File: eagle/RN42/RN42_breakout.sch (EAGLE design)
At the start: 15 parts

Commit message: Update RN42 breakout board.
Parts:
- removed U$3, U$4: N-CHANNEL-MOSFET-BSS138, GeekAmmo:N-CHANNEL-MOSFET-BSS138
- added L2, L3: (no value), led:LEDCHIPLED_0603
- added R6, R7: 1k, rcl:R-EU_R0603
- added SJ1, SJ2, SJ3, SJ4: (no value), jumper:SJ
- added T1: N-MOSFET, GeekAmmo:N-CHANNEL-MOSFET-BSS138
- added T2: N-CHANNEL-MOSFET-BSS138, GeekAmmo:N-CHANNEL-MOSFET-BSS138
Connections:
- removed net LINK: U$1.UARTCTS, U$1.UARTRTS
- new net AUTODISCOVERY: SJ3.1, U$1.PIO3
- new net BD_RATE: SJ4.1, U$1.PIO7
- new net BT_MASTER: SJ1.1, U$1.PIO6
- new net CTS: J1.3, U$1.UARTCTS
- new net N$3: L2.A, R6.2
- new net N$4: L3.A, R7.1
- new net RTS: J1.4, U$1.UARTRTS
- net 3V3: now also R7.2, SJ1.2, SJ3.2, SJ4.2, T1.G, T2.G; no longer U$3.G, U$4.G
- net GND: now also J1.1, L2.C, L3.C, SJ2.2; no longer J1.3, U$1.PIO7
- net RESET: now also SJ2.1; no longer J1.1
- net RX: now also T2.S; no longer U$3.S
- net RXH: now also T2.D; no longer U$3.D
- net STATUS: now also R6.1; no longer J1.4
- net TX: now also T1.S; no longer U$4.S
- net TXH: now also T1.D; no longer U$4.D
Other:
- note added: "Power Status"
- note added: "Reset (low power operation)"
- note added: "VCC to 3V3"
- moved on the sheet: L1, R1, R2, R3, R4, R5, U$1

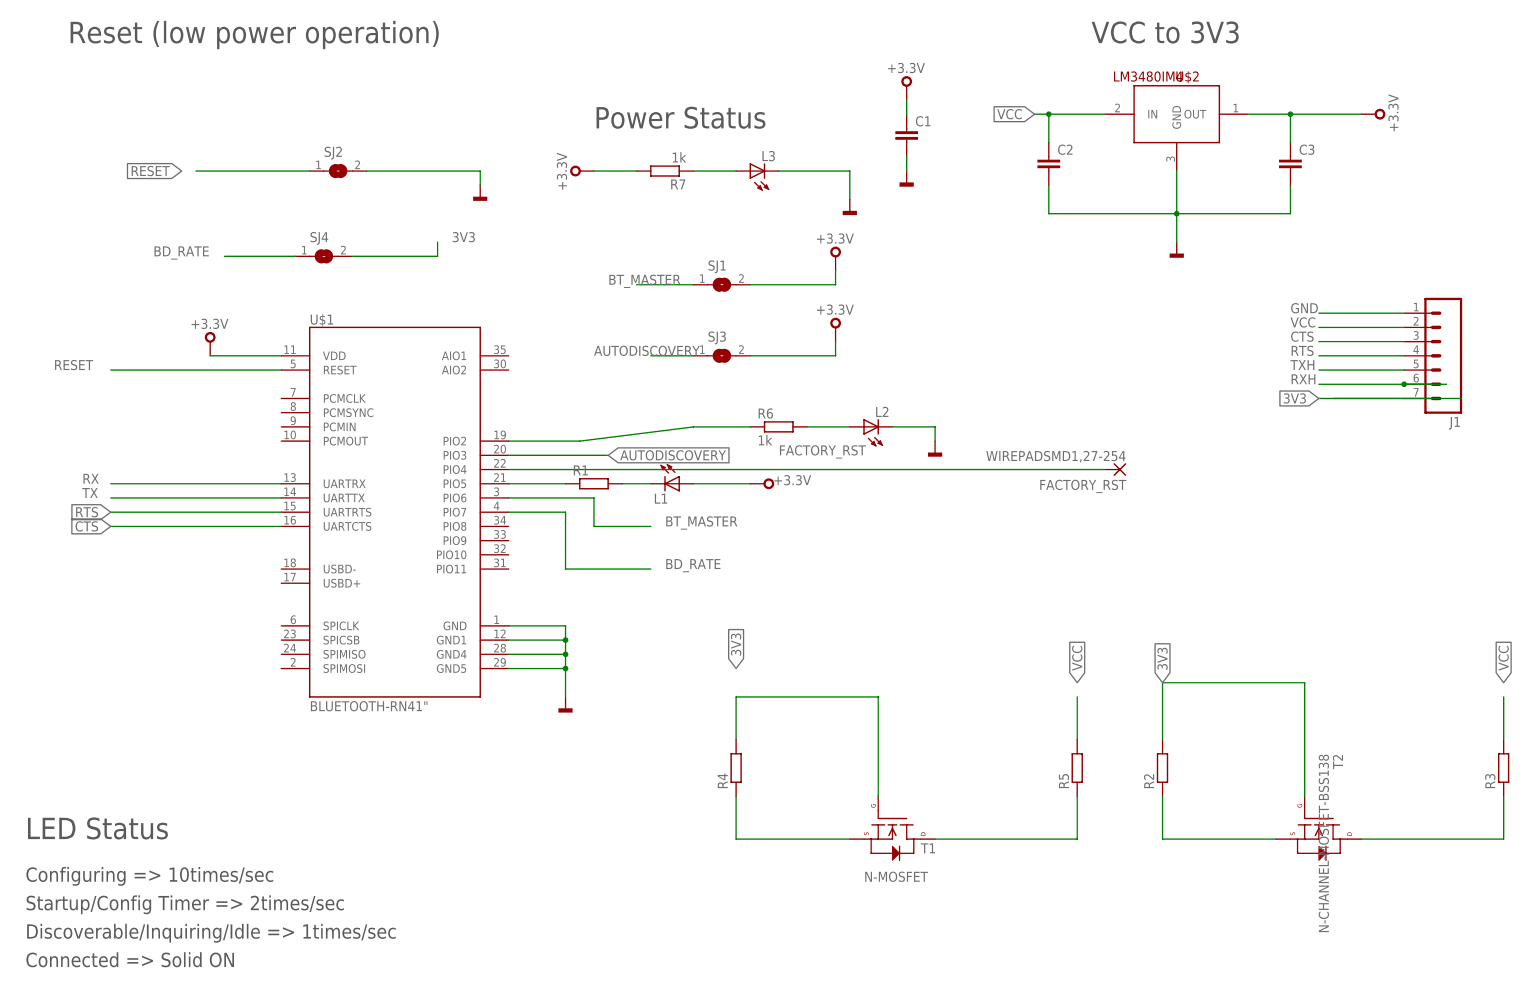
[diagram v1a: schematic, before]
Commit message: Pratically completed layout for RN42 breakout.
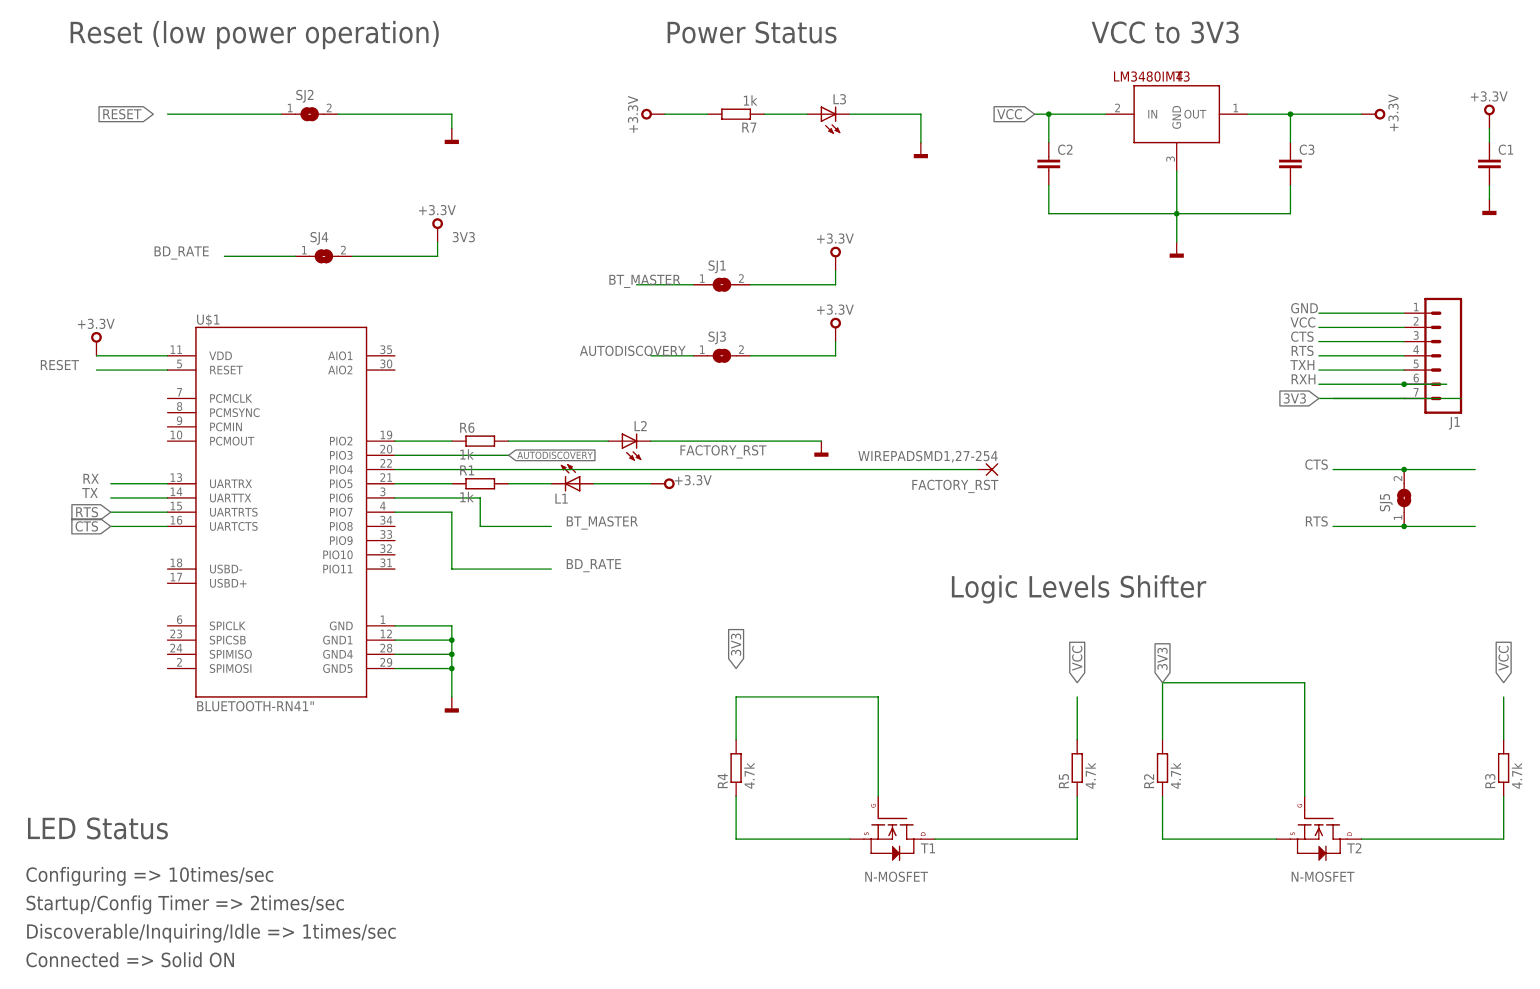
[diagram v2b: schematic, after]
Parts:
- added SJ5: (no value), jumper:SJ
- R1: value (none) -> 1k
- R2, R3, R4, R5: value (none) -> 4.7k
- T2: value N-CHANNEL-MOSFET-BSS138 -> N-MOSFET
- renumbered U$2 to T3
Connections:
- net CTS: now also SJ5.2
- net RTS: now also SJ5.1
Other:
- note added: "Logic Levels Shifter"
- moved on the sheet: C1, FACTORY_RST, L1, L2, L3, R1, R6, R7, SJ2, U$1

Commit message: Fix some labels on RN42 breakout.
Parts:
- renumbered L1 to STATUS, L2 to CONN, SJ1 to MASTER, SJ2 to POWER, SJ3 to AUTODISCOVERY, SJ4 to BAUD
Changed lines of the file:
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@@
 <part name="FACTORY_RST" library="wirepad" deviceset="WIREPAD" device="SMD1,27-254" value="WIREPADSMD1,27-254"/>
 <part name="U$1" library="SparkFun" deviceset="BLUETOOTH-RN41" device="&quot;"/>
-<part name="L1" library="led" deviceset="LED" device="CHIPLED_0603"/>
+<part name="STATUS" library="led" deviceset="LED" device="CHIPLED_0603"/>
 <part name="T3" library="SparkFun-PowerIC" deviceset="LM3480IM4" device=""/>
 <part name="C2" library="SparkFun-Passives" deviceset="CAP" device="0603-CAP"/>
@@
 </part>
 <part name="R6" library="rcl" deviceset="R-EU_" device="R0603" value="1k"/>
-<part name="L2" library="led" deviceset="LED" device="CHIPLED_0603"/>
+<part name="CONN" library="led" deviceset="LED" device="CHIPLED_0603"/>
 <part name="GND5" library="mbed-power" deviceset="GND" device=""/>
 <part name="U+3" library="mbed-power" deviceset="+3.3V" device=""/>
@@
 <part name="L3" library="led" deviceset="LED" device="CHIPLED_0603"/>
 <part name="GND7" library="mbed-power" deviceset="GND" device=""/>
-<part name="SJ1" library="jumper" deviceset="SJ" device=""/>
+<part name="MASTER" library="jumper" deviceset="SJ" device=""/>
 <part name="3V3" library="mbed-power" deviceset="+3.3V" device=""/>
-<part name="SJ2" library="jumper" deviceset="SJ" device=""/>
-<part name="SJ3" library="jumper" deviceset="SJ" device=""/>
+<part name="POWER" library="jumper" deviceset="SJ" device=""/>
+<part name="AUTODISCOVERY" library="jumper" deviceset="SJ" device=""/>
 <part name="3V1" library="mbed-power" deviceset="+3.3V" device=""/>
-<part name="SJ4" library="jumper" deviceset="SJ" device=""/>
+<part name="BAUD" library="jumper" deviceset="SJ" device=""/>
 <part name="SJ5" library="jumper" deviceset="SJ" device=""/>
 <part name="3V2" library="mbed-power" deviceset="+3.3V" device=""/>
@@
 </instance>
 <instance part="U$1" gate="G$1" x="55.88" y="101.6"/>
-<instance part="L1" gate="G$1" x="109.22" y="106.68" rot="R270"/>
+<instance part="STATUS" gate="G$1" x="109.22" y="106.68" rot="R270"/>
 <instance part="T3" gate="G$1" x="215.9" y="172.72"/>
 <instance part="C2" gate="G$1" x="193.04" y="162.56"/>
@@
 </instance>
 <instance part="R6" gate="G$1" x="91.44" y="114.3"/>
-<instance part="L2" gate="G$1" x="116.84" y="114.3" rot="R90"/>
+<instance part="CONN" gate="G$1" x="116.84" y="114.3" rot="R90"/>
 <instance part="GND5" gate="1" x="152.4" y="114.3"/>
 <instance part="U+3" gate="1" x="124.46" y="172.72" rot="R90"/>
@@
 <instance part="L3" gate="G$1" x="152.4" y="172.72" rot="R90"/>
 <instance part="GND7" gate="1" x="86.36" y="170.18"/>
-<instance part="SJ1" gate="1" x="134.62" y="142.24"/>
+<instance part="MASTER" gate="1" x="134.62" y="142.24"/>
 <instance part="3V3" gate="1" x="154.94" y="144.78"/>
-<instance part="SJ2" gate="1" x="60.96" y="172.72"/>
-<instance part="SJ3" gate="1" x="134.62" y="129.54"/>
+<instance part="POWER" gate="1" x="60.96" y="172.72"/>
+<instance part="AUTODISCOVERY" gate="1" x="134.62" y="129.54"/>
 <instance part="3V1" gate="1" x="154.94" y="132.08"/>
-<instance part="SJ4" gate="1" x="63.5" y="147.32"/>
+<instance part="BAUD" gate="1" x="63.5" y="147.32"/>
 <instance part="SJ5" gate="1" x="256.54" y="104.14" rot="R90"/>
 <instance part="3V2" gate="1" x="83.82" y="149.86"/>
@@
 <segment>
 <pinref part="GND5" gate="1" pin="GND"/>
-<pinref part="L2" gate="G$1" pin="C"/>
+<pinref part="CONN" gate="G$1" pin="C"/>
 <wire x1="121.92" y1="114.3" x2="152.4" y2="114.3" width="0.1524" layer="91"/>
 </segment>
@@
 <wire x1="86.36" y1="172.72" x2="86.36" y2="170.18" width="0.1524" layer="91"/>
 <pinref part="GND7" gate="1" pin="GND"/>
-<pinref part="SJ2" gate="1" pin="2"/>
+<pinref part="POWER" gate="1" pin="2"/>
 <wire x1="86.36" y1="172.72" x2="66.04" y2="172.72" width="0.1524" layer="91"/>
 </segment>
@@
 <wire x1="55.88" y1="172.72" x2="35.56" y2="172.72" width="0.1524" layer="91"/>
 <label x="33.02" y="172.72" size="1.778" layer="95" rot="R180" xref="yes"/>
-<pinref part="SJ2" gate="1" pin="1"/>
+<pinref part="POWER" gate="1" pin="1"/>
 </segment>
 </net>
@@
 <wire x1="104.14" y1="106.68" x2="96.52" y2="106.68" width="0.1524" layer="91"/>
 <pinref part="R1" gate="G$1" pin="2"/>
-<pinref part="L1" gate="G$1" pin="C"/>
+<pinref part="STATUS" gate="G$1" pin="C"/>
 </segment>
 </net>
@@
 <wire x1="121.92" y1="106.68" x2="111.76" y2="106.68" width="0.1524" layer="91"/>
 <pinref part="U+2" gate="1" pin="+3,3V"/>
-<pinref part="L1" gate="G$1" pin="A"/>
+<pinref part="STATUS" gate="G$1" pin="A"/>
 </segment>
 <segment>
@@
 </segment>
 <segment>
-<pinref part="SJ1" gate="1" pin="2"/>
+<pinref part="MASTER" gate="1" pin="2"/>
 <wire x1="139.7" y1="142.24" x2="154.94" y2="142.24" width="0.1524" layer="91"/>
 <wire x1="154.94" y1="142.24" x2="154.94" y2="144.78" width="0.1524" layer="91"/>
@@
 </segment>
 <segment>
-<pinref part="SJ3" gate="1" pin="2"/>
+<pinref part="AUTODISCOVERY" gate="1" pin="2"/>
 <wire x1="139.7" y1="129.54" x2="154.94" y2="129.54" width="0.1524" layer="91"/>
 <wire x1="154.94" y1="129.54" x2="154.94" y2="132.08" width="0.1524" layer="91"/>
@@
 </segment>
 <segment>
-<pinref part="SJ4" gate="1" pin="2"/>
+<pinref part="BAUD" gate="1" pin="2"/>
 <wire x1="68.58" y1="147.32" x2="83.82" y2="147.32" width="0.1524" layer="91"/>
 <wire x1="83.82" y1="147.32" x2="83.82" y2="149.86" width="0.1524" layer="91"/>
@@
 <segment>
 <pinref part="R6" gate="G$1" pin="2"/>
-<pinref part="L2" gate="G$1" pin="A"/>
+<pinref part="CONN" gate="G$1" pin="A"/>
 <wire x1="96.52" y1="114.3" x2="114.3" y2="114.3" width="0.1524" layer="91"/>
 </segment>
@@
 </segment>
 <segment>
-<pinref part="SJ3" gate="1" pin="1"/>
+<pinref part="AUTODISCOVERY" gate="1" pin="1"/>
 <wire x1="129.54" y1="129.54" x2="121.92" y2="129.54" width="0.1524" layer="91"/>
 <label x="109.22" y="129.54" size="1.778" layer="95"/>
@@
 </segment>
 <segment>
-<pinref part="SJ1" gate="1" pin="1"/>
+<pinref part="MASTER" gate="1" pin="1"/>
 <wire x1="129.54" y1="142.24" x2="119.38" y2="142.24" width="0.1524" layer="91"/>
 <label x="114.3" y="142.24" size="1.778" layer="95"/>
@@
 </segment>
 <segment>
-<pinref part="SJ4" gate="1" pin="1"/>
+<pinref part="BAUD" gate="1" pin="1"/>
 <wire x1="58.42" y1="147.32" x2="45.72" y2="147.32" width="0.1524" layer="91"/>
 <label x="33.02" y="147.32" size="1.778" layer="95"/>

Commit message: Complete first release
Add production file.
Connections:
- net CTS: no longer J1.3
- net GND: now also J1.3; no longer J1.1
- net RTS: no longer J1.4
- net VCC: now also J1.4; no longer J1.2
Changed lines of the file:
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@@
 </segment>
 <segment>
-<pinref part="J1" gate="G$1" pin="1"/>
-<wire x1="256.54" y1="137.16" x2="241.3" y2="137.16" width="0.1524" layer="91"/>
+<pinref part="J1" gate="G$1" pin="3"/>
+<wire x1="256.54" y1="132.08" x2="241.3" y2="137.16" width="0.1524" layer="91"/>
 <label x="236.22" y="137.16" size="1.778" layer="95"/>
 </segment>
@@
 </segment>
 <segment>
-<pinref part="J1" gate="G$1" pin="4"/>
-<wire x1="256.54" y1="129.54" x2="241.3" y2="129.54" width="0.1524" layer="91"/>
-<label x="236.22" y="129.54" size="1.778" layer="95"/>
-</segment>
-<segment>
 <pinref part="SJ5" gate="1" pin="1"/>
 <wire x1="243.84" y1="99.06" x2="256.54" y2="99.06" width="0.1524" layer="91"/>
-<wire x1="256.54" y1="99.06" x2="269.24" y2="99.06" width="0.1524" layer="91"/>
-<junction x="256.54" y="99.06"/>
 <label x="238.76" y="99.06" size="1.778" layer="95"/>
 </segment>
@@
 </segment>
 <segment>
-<pinref part="J1" gate="G$1" pin="2"/>
-<wire x1="256.54" y1="134.62" x2="241.3" y2="134.62" width="0.1524" layer="91"/>
+<pinref part="J1" gate="G$1" pin="4"/>
+<wire x1="256.54" y1="129.54" x2="241.3" y2="134.62" width="0.1524" layer="91"/>
 <label x="236.22" y="134.62" size="1.778" layer="95"/>
 </segment>
@@
 <pinref part="J1" gate="G$1" pin="7"/>
 <wire x1="256.54" y1="121.92" x2="243.84" y2="121.92" width="0.1524" layer="91"/>
-<wire x1="256.54" y1="121.92" x2="266.7" y2="121.92" width="0.1524" layer="91"/>
 <wire x1="256.54" y1="121.92" x2="241.3" y2="121.92" width="0.1524" layer="91"/>
 <label x="241.3" y="121.92" size="1.778" layer="95" rot="R180" xref="yes"/>
@@
 <net name="RXH" class="0">
 <segment>
-<wire x1="264.16" y1="124.46" x2="256.54" y2="124.46" width="0.1524" layer="91"/>
 <label x="236.22" y="124.46" size="1.778" layer="95"/>
 <pinref part="J1" gate="G$1" pin="6"/>
-<junction x="256.54" y="124.46"/>
 <wire x1="256.54" y1="124.46" x2="241.3" y2="124.46" width="0.1524" layer="91"/>
 </segment>
@@
 </segment>
 <segment>
-<pinref part="J1" gate="G$1" pin="3"/>
-<wire x1="256.54" y1="132.08" x2="241.3" y2="132.08" width="0.1524" layer="91"/>
-<label x="236.22" y="132.08" size="1.778" layer="95"/>
-</segment>
-<segment>
 <pinref part="SJ5" gate="1" pin="2"/>
 <wire x1="243.84" y1="109.22" x2="256.54" y2="109.22" width="0.1524" layer="91"/>
-<wire x1="256.54" y1="109.22" x2="269.24" y2="109.22" width="0.1524" layer="91"/>
-<junction x="256.54" y="109.22"/>
 <label x="238.76" y="109.22" size="1.778" layer="95"/>
 </segment>

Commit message: RN42: update some values.
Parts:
- C1: value (none) -> 1uF
- C2, C3: value (none) -> 0.1uF
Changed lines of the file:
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@@
 <?xml version="1.0" encoding="utf-8"?>
 <!DOCTYPE eagle SYSTEM "eagle.dtd">
-<eagle version="7.2.0">
+<eagle version="7.5.0">
 <drawing>
 <settings>
@@
 <part name="R1" library="rcl" deviceset="R-EU_" device="R0603" value="1k"/>
 <part name="U+2" library="mbed-power" deviceset="+3.3V" device=""/>
-<part name="C1" library="rcl" deviceset="C-EU" device="C0603"/>
+<part name="C1" library="rcl" deviceset="C-EU" device="C0603" value="1uF"/>
 <part name="GND2" library="mbed-power" deviceset="GND" device=""/>
 <part name="U+4" library="mbed-power" deviceset="+3.3V" device=""/>
@@
 <part name="STATUS" library="led" deviceset="LED" device="CHIPLED_0603"/>
 <part name="T3" library="SparkFun-PowerIC" deviceset="LM3480IM4" device=""/>
-<part name="C2" library="SparkFun-Passives" deviceset="CAP" device="0603-CAP"/>
-<part name="C3" library="SparkFun-Passives" deviceset="CAP" device="0603-CAP"/>
+<part name="C2" library="SparkFun-Passives" deviceset="CAP" device="0603-CAP" value="0.1uF"/>
+<part name="C3" library="SparkFun-Passives" deviceset="CAP" device="0603-CAP" value="0.1uF"/>
 <part name="GND4" library="mbed-power" deviceset="GND" device=""/>
 <part name="U+5" library="mbed-power" deviceset="+3.3V" device=""/>

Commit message: RN42: add datasheet.
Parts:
- T1: DATASHEET (none) -> http://www.onsemi.com/pub/Collateral/NTR4501N-D.PDF
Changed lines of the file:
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@@
 <part name="R2" library="rcl" deviceset="R-EU_" device="R0603" value="4.7k"/>
 <part name="R3" library="rcl" deviceset="R-EU_" device="R0603" value="4.7k"/>
-<part name="T1" library="GeekAmmo" deviceset="N-CHANNEL-MOSFET" device="-BSS138" value="N-MOSFET"/>
+<part name="T1" library="GeekAmmo" deviceset="N-CHANNEL-MOSFET" device="-BSS138" value="N-MOSFET">
+<attribute name="DATASHEET" value="http://www.onsemi.com/pub/Collateral/NTR4501N-D.PDF"/>
+</part>
 <part name="R4" library="rcl" deviceset="R-EU_" device="R0603" value="4.7k"/>
 <part name="R5" library="rcl" deviceset="R-EU_" device="R0603" value="4.7k"/>
@@
 <attribute name="VALUE" x="160.02" y="35.56" size="1.778" layer="96"/>
 <attribute name="NAME" x="170.18" y="40.64" size="1.778" layer="95"/>
+<attribute name="URL" x="165.1" y="45.72" size="1.778" layer="96" rot="R270" display="off"/>
 </instance>
 <instance part="R4" gate="G$1" x="137.16" y="55.88" rot="R90"/>
